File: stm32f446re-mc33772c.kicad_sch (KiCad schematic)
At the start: 20 parts, among them J1 Conn_01x02, U1 STM32F446RETx, U3 LD1086D2M33TR, Y1 16MHz

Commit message: feat: STM32F446RE basically done, MC33772C remains
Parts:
- added C15, C16: 22u, Capacitor_SMD:C_0402_1005Metric, symbol Device:C
- added J2: USB_B_Micro, symbol Connector:USB_B_Micro
- added J3: Conn_01x03, symbol Connector_Generic:Conn_01x03
- added J4: Conn_01x06, symbol Connector_Generic:Conn_01x06
- added R3: 1k5, Resistor_SMD:R_0805_2012Metric, symbol Device:R
- added U4: AMS1117-3.3, Package_TO_SOT_SMD:SOT-223-3_TabPin2, symbol Regulator_Linear:AMS1117-3.3
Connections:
- net GND: now also C15.2, C16.2, J2.5 (GND), J2.SH (Shield), J4.2 (Pin_2), U4.1 (GND)
- net LDO_3.3V: now also J3.2 (Pin_2), J4.1 (Pin_1), R3.2; no longer C5.1, U3.2 (OUT)
- net SWCLK: now also J4.4 (Pin_4)
- net SWDIO: now also J4.3 (Pin_3)
- net nRST: now reaches C1.2, U1.7 (NRST)
- net nRST: now also J4.5 (Pin_5)
- net D-: now reaches U1.44 (PA11)
- net D-: now also J2.2 (D-)
- net D+: now reaches U1.45 (PA12)
- net D+: now also J2.3 (D+), R3.1
- net SWO: now reaches U1.55 (PB3)
- net SWO: now also J4.6 (Pin_6)
- net VBAT+ renamed VBAT_24V
- new net BAT_3.3V: C5.1, J3.1 (Pin_1), U3.2 (OUT)
- new net USB_3.3V: C16.1, J3.3 (Pin_3), U4.2 (VO)
- new net VBUS_5V: C15.1, J2.1 (VBUS), U4.3 (VI)
- no-connect marks 42 -> 40
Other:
- note added: "Connect to ST Link V2/V3 external USB stick"
- note added: "Jumper: choose between battery or USB."

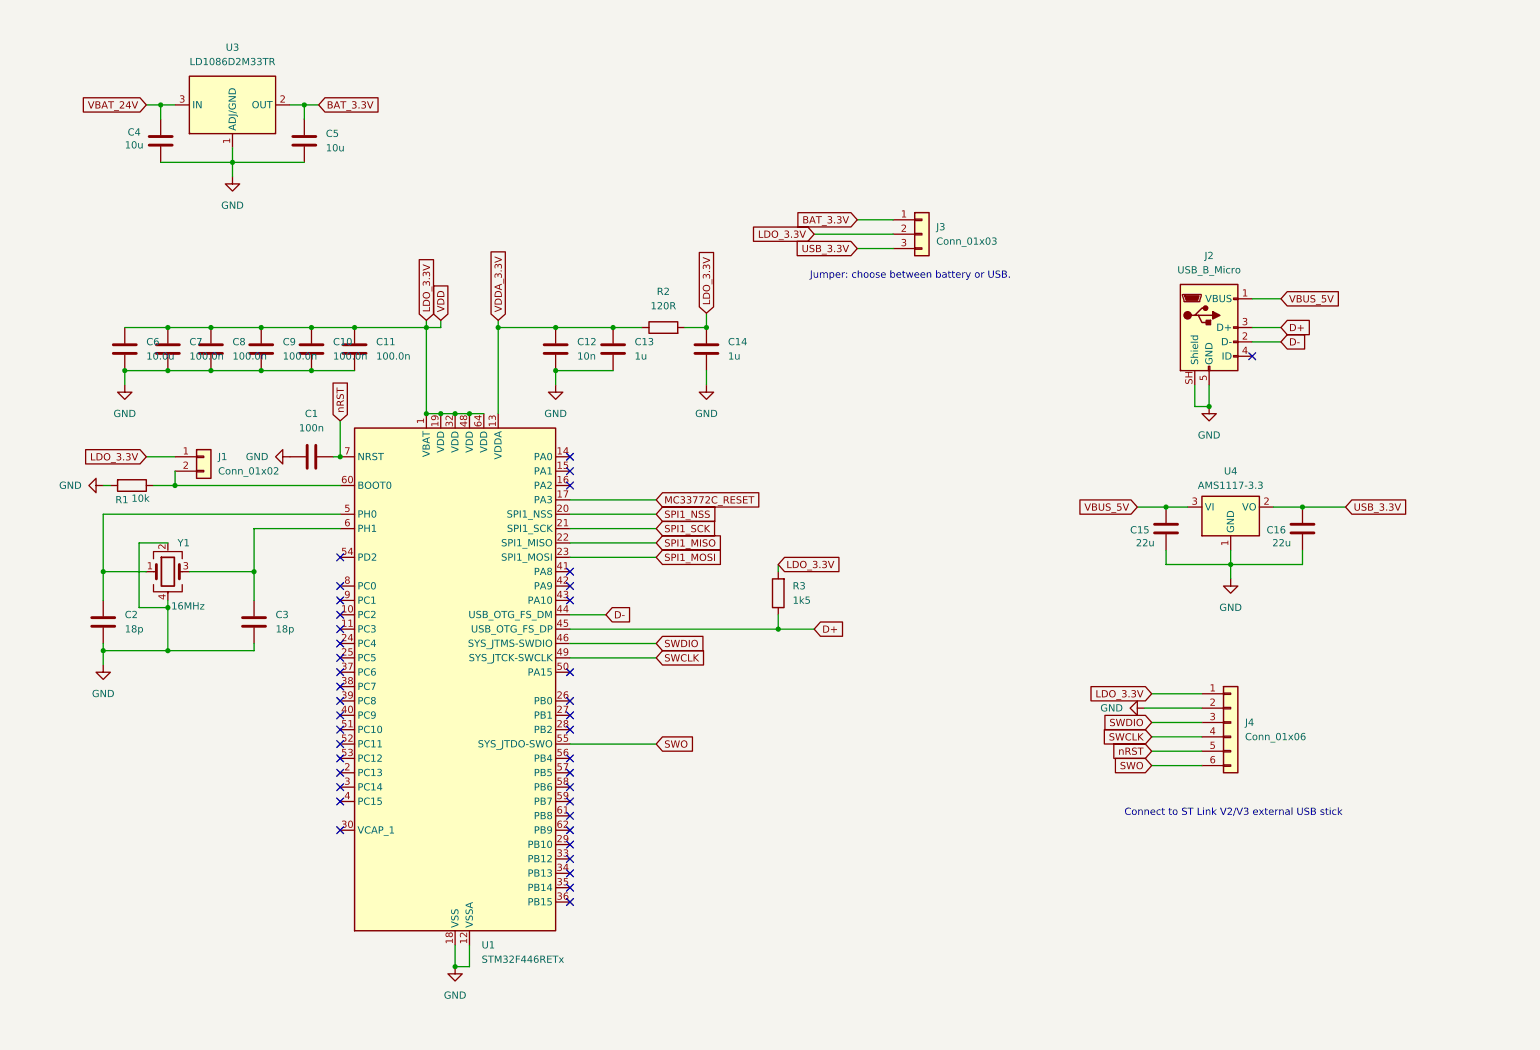
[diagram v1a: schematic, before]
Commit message: feat: CAN/BUCK
1. CAN transceiver added
2. Buck added 24V -> 5V
3. LDO 5V -> 3.3V
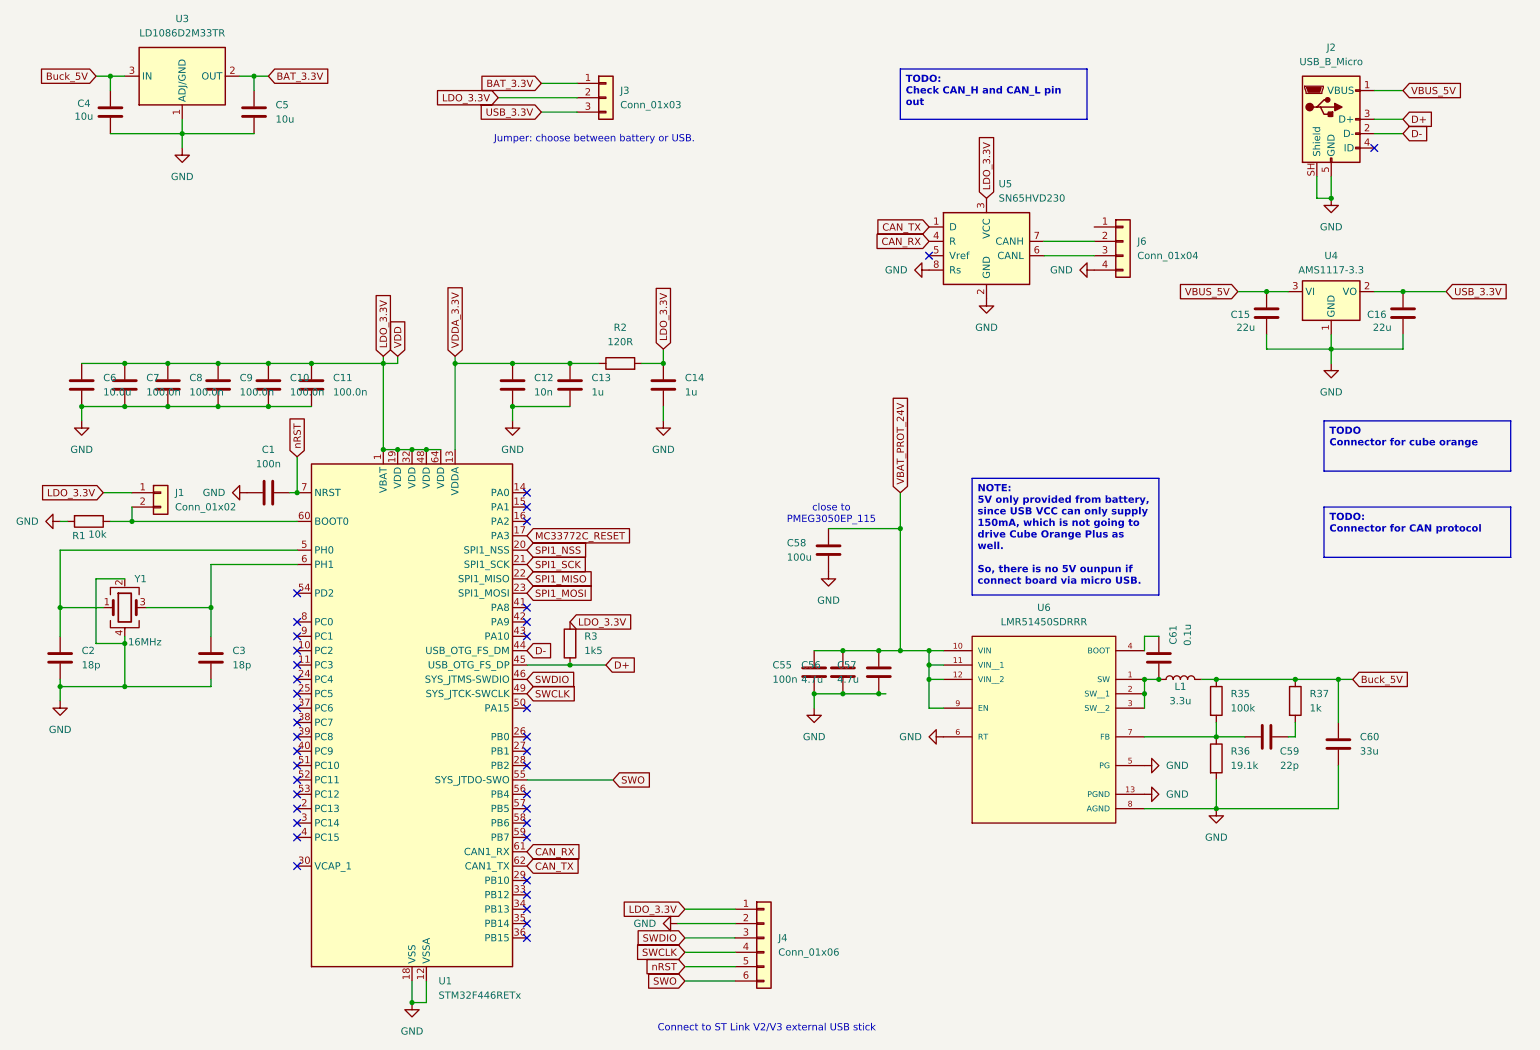
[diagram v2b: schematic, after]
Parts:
- added C55: 100n, Capacitor_SMD:C_0402_1005Metric, symbol Device:C
- added C56, C57: 4.7u, Capacitor_SMD:C_1210_3225Metric, symbol Device:C
- added C58: 100u, symbol Device:C
- added C59: 22p, symbol Device:C
- added C60: 33u, symbol Device:C
- added C61: 0.1u, symbol Device:C
- added J6: Conn_01x04, Connector_JST:JST_XH_S4B-XH-A_1x04_P2.50mm_Horizontal, symbol Connector_Generic:Conn_01x04
- added L1: 3.3u, symbol Device:L
- added R35: 100k, symbol Device:R
- added R36: 19.1k, symbol Device:R
- added R37: 1k, symbol Device:R
- added U5: SN65HVD230, Package_SO:SOIC-8_3.9x4.9mm_P1.27mm, symbol Interface_CAN_LIN:SN65HVD230
- added U6: LMR51450SDRRR, LMR51450SDRRR:CONV_LMR51450SDRRR, symbol LMR51450SDRRR:LMR51450SDRRR
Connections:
- net GND: now also C55.2, C56.2, C57.2, C58.2, C60.2, J6.4 (Pin_4), R36.2, U5.2 (GND), U5.8 (Rs), U6.13 (PGND), U6.5 (PG), U6.6 (RT), U6.8 (AGND)
- net LDO_3.3V: now also U5.3 (VCC)
- net CAN_RX: now reaches U1.61 (PB8)
- net CAN_RX: now also U5.4 (R)
- net CAN_TX: now reaches U1.62 (PB9)
- net CAN_TX: now also U5.1 (D)
- net VBAT_24V renamed Buck_5V
- net Buck_5V: now also C60.1, L1.2, R35.1, R37.1
- new net: C61.1, U6.4 (BOOT)
- new net: C61.2, L1.1, U6.1 (SW), U6.2 (SW__1), U6.3 (SW__2)
- new net: J6.2 (Pin_2), U5.7 (CANH)
- new net: J6.3 (Pin_3), U5.6 (CANL)
- new net: C59.2, R35.2, R36.1, U6.7 (FB)
- new net: C59.1, R37.2
- new net VBAT_PROT_24V: C55.1, C56.1, C57.1, C58.1, U6.10 (VIN), U6.11 (VIN__1), U6.12 (VIN__2), U6.9 (EN)
- no-connect marks 40 -> 39
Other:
- note added: "close to PMEG3050EP_115"
- moved on the sheet: C1, C10, C11, C12, C13, C14, C15, C16, C2, C3, C4, C5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

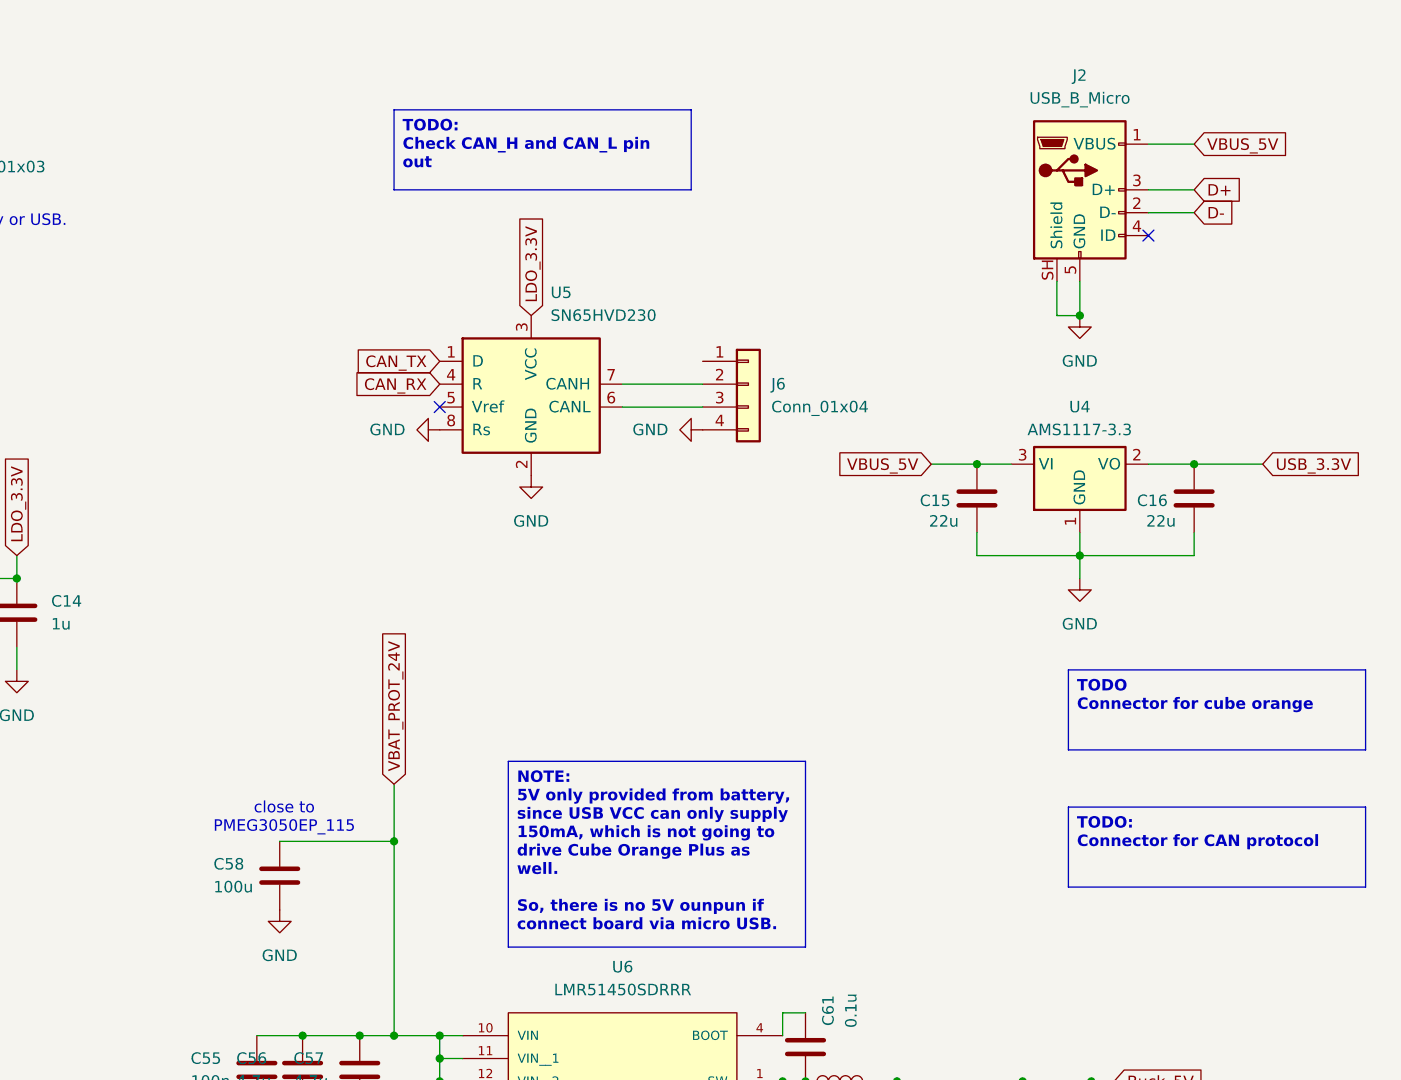
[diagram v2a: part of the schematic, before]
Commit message: CAN/BUCK/CONNECTOR done
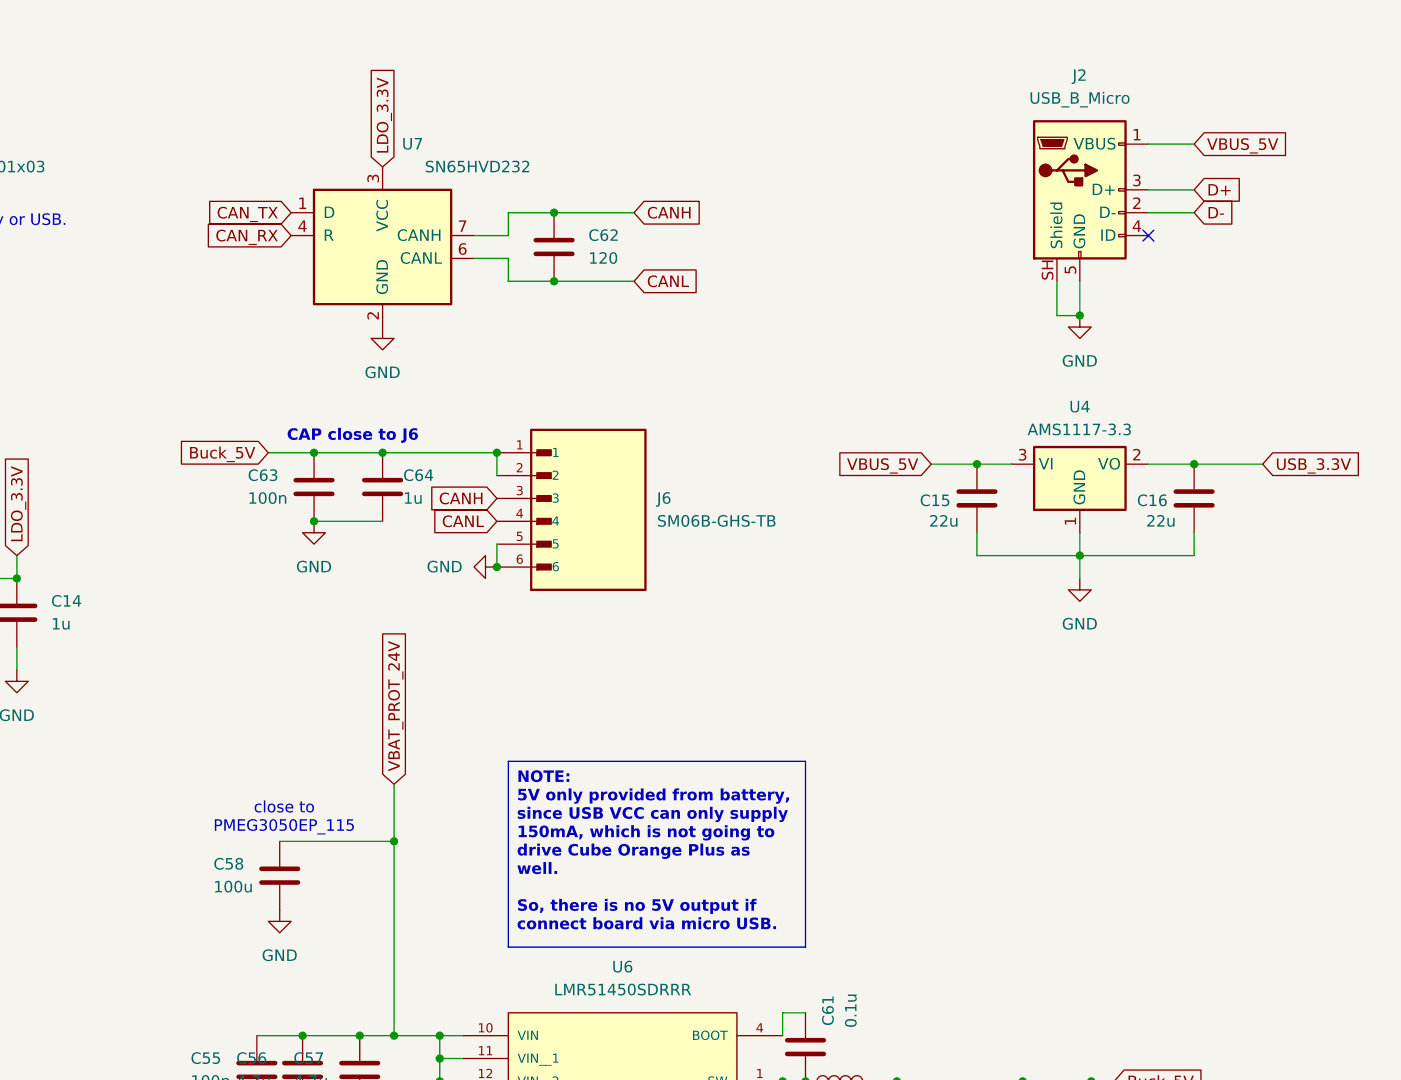
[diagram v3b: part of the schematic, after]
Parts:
- removed J6: Conn_01x04, Connector_JST:JST_XH_S4B-XH-A_1x04_P2.50mm_Horizontal, symbol Connector_Generic:Conn_01x04
- removed U5: SN65HVD230, Package_SO:SOIC-8_3.9x4.9mm_P1.27mm, symbol Interface_CAN_LIN:SN65HVD230
- added C62: 120, symbol Device:C
- added C63: 100n, Capacitor_SMD:C_0402_1005Metric, symbol Device:C
- added C64: 1u, Capacitor_SMD:C_0603_1608Metric, symbol Device:C
- added J6: SM06B-GHS-TB, SM06B-GHS-TB:JST_SM06B-GHS-TB, symbol SM06B-GHS-TB:SM06B-GHS-TB
- added U7: SN65HVD232, Package_SO:SOIC-8_3.9x4.9mm_P1.27mm, symbol Interface_CAN_LIN:SN65HVD232
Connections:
- net Buck_5V: now also C63.1, C64.1, J6.1, J6.2
- net CAN_RX: now also U7.4 (R)
- net CAN_TX: now also U7.1 (D)
- net GND: now also C63.2, C64.2, J6.5, J6.6, U7.2 (GND)
- net LDO_3.3V: now also U7.3 (VCC)
- new net CANH: C62.1, J6.3, U7.7 (CANH)
- new net CANL: C62.2, J6.4, U7.6 (CANL)
- no-connect marks 39 -> 38
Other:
- note added: "CAP close to J6"
